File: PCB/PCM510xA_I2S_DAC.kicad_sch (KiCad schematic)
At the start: 30 parts, among them J1 EDGE_PINS, J2 TRS_LINE_OUT, U1 PCM5101A, U2 MIC5225-3.3

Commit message: update to 1.0.0
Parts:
- removed JP1: SCK, Jumper:SolderJumper-3_P1.3mm_Bridged12_RoundedPad1.0x1.5mm, symbol Jumper:SolderJumper_3_Bridged12
- removed TP4: 3.3VA, TestPoint:TestPoint_Pad_2.0x2.0mm, symbol Connector:TestPoint
- removed TP5: LDOO, TestPoint:TestPoint_Pad_2.0x2.0mm, symbol Connector:TestPoint
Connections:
- net SCK is gone; now on net GND: U1.12 (SCK)
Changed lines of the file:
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@@
   (title_block
     (title "PCM510x_I2S_DAC Breakout")
-    (date "2023-10-02")
-    (rev "0.0.2")
+    (date "2023-10-22")
+    (rev "1.0.0")
     (company "Cedar Grove Studios")
   )
@@
   (junction (at 59.69 185.42) (diameter 0) (color 0 0 0 0)
   )
-  (junction (at 148.59 106.68) (diameter 0) (color 0 0 0 0)
-  )
   (junction (at 65.405 167.64) (diameter 0) (color 0 0 0 0)
   )
@@
   )
   (junction (at 194.945 73.66) (diameter 0) (color 0 0 0 0)
+  )
+  (junction (at 111.125 82.55) (diameter 0) (color 0 0 0 0)
   )
   (junction (at 137.16 182.245) (diameter 0) (color 0 0 0 0)
@@
     (stroke (width 0) (type default))
   )
-  (wire (pts (xy 100.965 121.285) (xy 100.965 127.635))
-    (stroke (width 0) (type default))
-  )
   (wire (pts (xy 182.88 89.535) (xy 180.34 89.535))
     (stroke (width 0) (type default))
@@
     (stroke (width 0) (type default))
   )
+  (wire (pts (xy 111.125 82.55) (xy 111.125 77.47))
+    (stroke (width 0) (type default))
+  )
   (wire (pts (xy 148.59 106.68) (xy 157.48 106.68))
     (stroke (width 0) (type default))
@@
     (stroke (width 0) (type default))
   )
+  (wire (pts (xy 111.125 77.47) (xy 124.46 77.47))
+    (stroke (width 0) (type default))
+  )
   (wire (pts (xy 29.845 185.42) (xy 34.29 185.42))
     (stroke (width 0) (type default))
@@
     (stroke (width 0) (type default))
   )
-  (wire (pts (xy 104.775 77.47) (xy 124.46 77.47))
-    (stroke (width 0) (type default))
-  )
   (wire (pts (xy 149.86 72.39) (xy 170.815 72.39))
     (stroke (width 0) (type default))
@@
     (stroke (width 0) (type default))
   )
-  (wire (pts (xy 104.775 77.47) (xy 104.775 116.205))
-    (stroke (width 0) (type default))
-  )
   (wire (pts (xy 170.815 89.535) (xy 175.26 89.535))
     (stroke (width 0) (type default))
@@
   )
   (wire (pts (xy 124.46 87.63) (xy 120.015 87.63))
-    (stroke (width 0) (type default))
-  )
-  (wire (pts (xy 100.965 104.775) (xy 100.965 111.125))
     (stroke (width 0) (type default))
   )
@@
   (label "DIN" (at 93.98 72.39 180) (fields_autoplaced)
     (effects (font (size 1.27 1.27)) (justify right bottom))
-  )
-  (label "SCK" (at 104.775 77.47 0) (fields_autoplaced)
-    (effects (font (size 1.27 1.27)) (justify left bottom))
   )
   (label "Vin" (at 21.59 167.64 0) (fields_autoplaced)
@@
     )
   )
-  (symbol (lib_id "power:GND") (at 100.965 127.635 0) (unit 1)
-    (in_bom yes) (on_board yes) (dnp no)
-    (property "Reference" "#PWR013" (at 100.965 133.985 0)
-      (effects (font (size 1.27 1.27)) hide)
-    )
-    (property "Value" "GND" (at 101.092 132.0292 0)
-      (effects (font (size 1.27 1.27)))
-    )
-    (property "Footprint" "" (at 100.965 127.635 0)
-      (effects (font (size 1.27 1.27)) hide)
-    )
-    (property "Datasheet" "" (at 100.965 127.635 0)
-      (effects (font (size 1.27 1.27)) hide)
-    )
-    (pin "1")
-    (instances
-      (project "PCM510xA_I2S_DAC"
-        (path "/d1262c4d-2245-4c4f-8f35-7bb32cd9e21e"
-          (reference "#PWR013") (unit 1)
-        )
-      )
-    )
-  )
   (symbol (lib_id "power:+3.3VA") (at 113.03 162.56 0) (unit 1)
     (in_bom yes) (on_board yes) (dnp no) (fields_autoplaced)
@@
         (path "/d1262c4d-2245-4c4f-8f35-7bb32cd9e21e"
           (reference "#PWR016") (unit 1)
-        )
-      )
-    )
-  )
-  (symbol (lib_id "Connector:TestPoint") (at 105.41 167.64 0) (unit 1)
-    (in_bom yes) (on_board yes) (dnp no) (fields_autoplaced)
-    (property "Reference" "TP4" (at 106.807 163.1259 0)
-      (effects (font (size 1.27 1.27)) (justify left))
-    )
-    (property "Value" "3.3VA" (at 106.807 165.5501 0)
-      (effects (font (size 1.27 1.27)) (justify left))
-    )
-    (property "Footprint" "TestPoint:TestPoint_Pad_2.0x2.0mm" (at 110.49 167.64 0)
-      (effects (font (size 1.27 1.27)) hide)
-    )
-    (property "Datasheet" "~" (at 110.49 167.64 0)
-      (effects (font (size 1.27 1.27)) hide)
-    )
-    (pin "1")
-    (instances
-      (project "PCM510xA_I2S_DAC"
-        (path "/d1262c4d-2245-4c4f-8f35-7bb32cd9e21e"
-          (reference "TP4") (unit 1)
         )
       )
@@
     )
   )
-  (symbol (lib_id "Connector:TestPoint") (at 148.59 106.68 0) (unit 1)
-    (in_bom yes) (on_board yes) (dnp no) (fields_autoplaced)
-    (property "Reference" "TP5" (at 149.987 102.1659 0)
-      (effects (font (size 1.27 1.27)) (justify left))
-    )
-    (property "Value" "LDOO" (at 149.987 104.5901 0)
-      (effects (font (size 1.27 1.27)) (justify left))
-    )
-    (property "Footprint" "TestPoint:TestPoint_Pad_2.0x2.0mm" (at 153.67 106.68 0)
-      (effects (font (size 1.27 1.27)) hide)
-    )
-    (property "Datasheet" "~" (at 153.67 106.68 0)
-      (effects (font (size 1.27 1.27)) hide)
-    )
-    (pin "1")
-    (instances
-      (project "PCM510xA_I2S_DAC"
-        (path "/d1262c4d-2245-4c4f-8f35-7bb32cd9e21e"
-          (reference "TP5") (unit 1)
-        )
-      )
-    )
-  )
   (symbol (lib_id "power:GND") (at 83.185 190.5 0) (unit 1)
     (in_bom yes) (on_board yes) (dnp no)
@@
     )
   )
-  (symbol (lib_id "Jumper:SolderJumper_3_Bridged12") (at 100.965 116.205 90) (unit 1)
-    (in_bom yes) (on_board yes) (dnp no) (fields_autoplaced)
-    (property "Reference" "JP1" (at 99.3141 114.9929 90)
-      (effects (font (size 1.27 1.27)) (justify left))
-    )
-    (property "Value" "SCK" (at 99.3141 117.4171 90)
-      (effects (font (size 1.27 1.27)) (justify left))
-    )
-    (property "Footprint" "Jumper:SolderJumper-3_P1.3mm_Bridged12_RoundedPad1.0x1.5mm" (at 100.965 116.205 0)
-      (effects (font (size 1.27 1.27)) hide)
-    )
-    (property "Datasheet" "~" (at 100.965 116.205 0)
-      (effects (font (size 1.27 1.27)) hide)
-    )
-    (pin "1")
-    (pin "2")
-    (pin "3")
-    (instances
-      (project "PCM510xA_I2S_DAC"
-        (path "/d1262c4d-2245-4c4f-8f35-7bb32cd9e21e"
-          (reference "JP1") (unit 1)
-        )
-      )
-    )
-  )
   (symbol (lib_id "power:+3.3VA") (at 161.925 40.64 0) (unit 1)
     (in_bom yes) (on_board yes) (dnp no) (fields_autoplaced)
@@
         )
       )
-    )
-  )
-  (symbol (lib_id "power:+3.3V") (at 100.965 104.775 0) (unit 1)
-    (in_bom yes) (on_board yes) (dnp no) (fields_autoplaced)
-    (property "Reference" "#PWR011" (at 100.965 108.585 0)
-      (effects (font (size 1.27 1.27)) hide)
-    )
-    (property "Value" "+3.3V" (at 100.965 100.6419 0)
-      (effects (font (size 1.27 1.27)))
-    )
-    (property "Footprint" "" (at 100.965 104.775 0)
-      (effects (font (size 1.27 1.27)) hide)
-    )
-    (property "Datasheet" "" (at 100.965 104.775 0)
-      (effects (font (size 1.27 1.27)) hide)
-    )
-    (pin "1")
-    (instances
-      (project "PCM510xA_I2S_DAC"
-        (path "/d1262c4d-2245-4c4f-8f35-7bb32cd9e21e"
-          (reference "#PWR011") (unit 1)
-        )
-      )

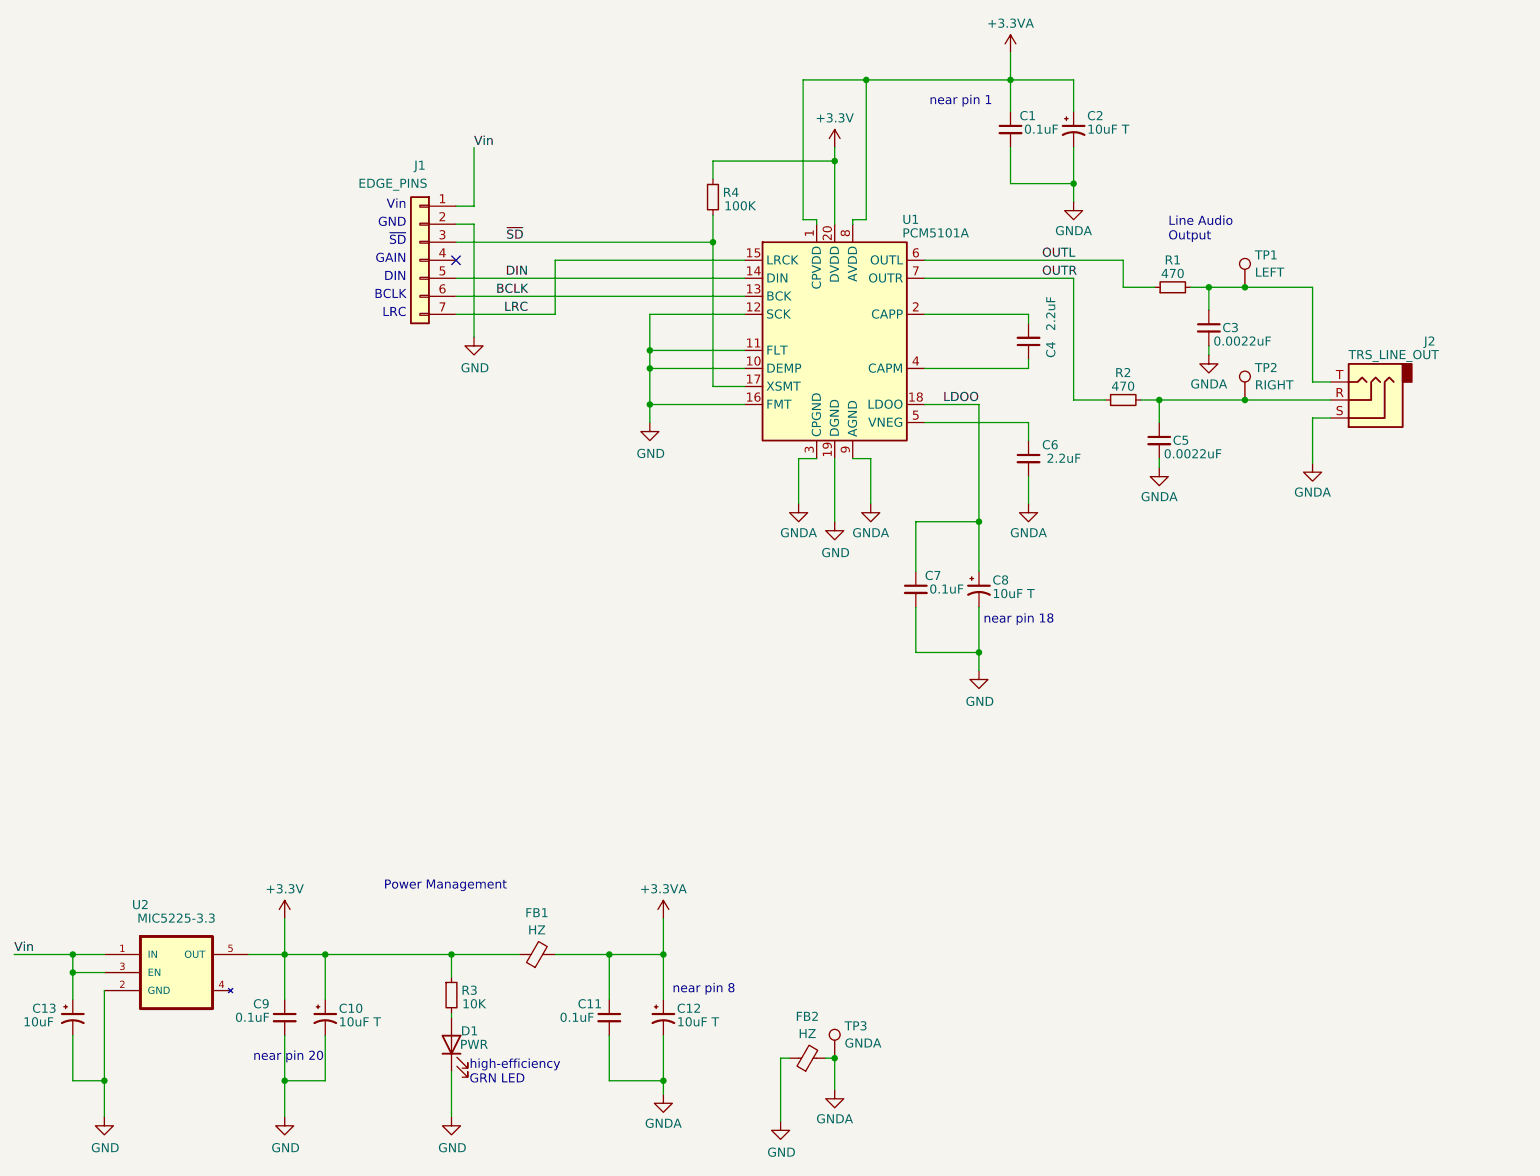
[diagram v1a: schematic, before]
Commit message: update 3.3v regulator
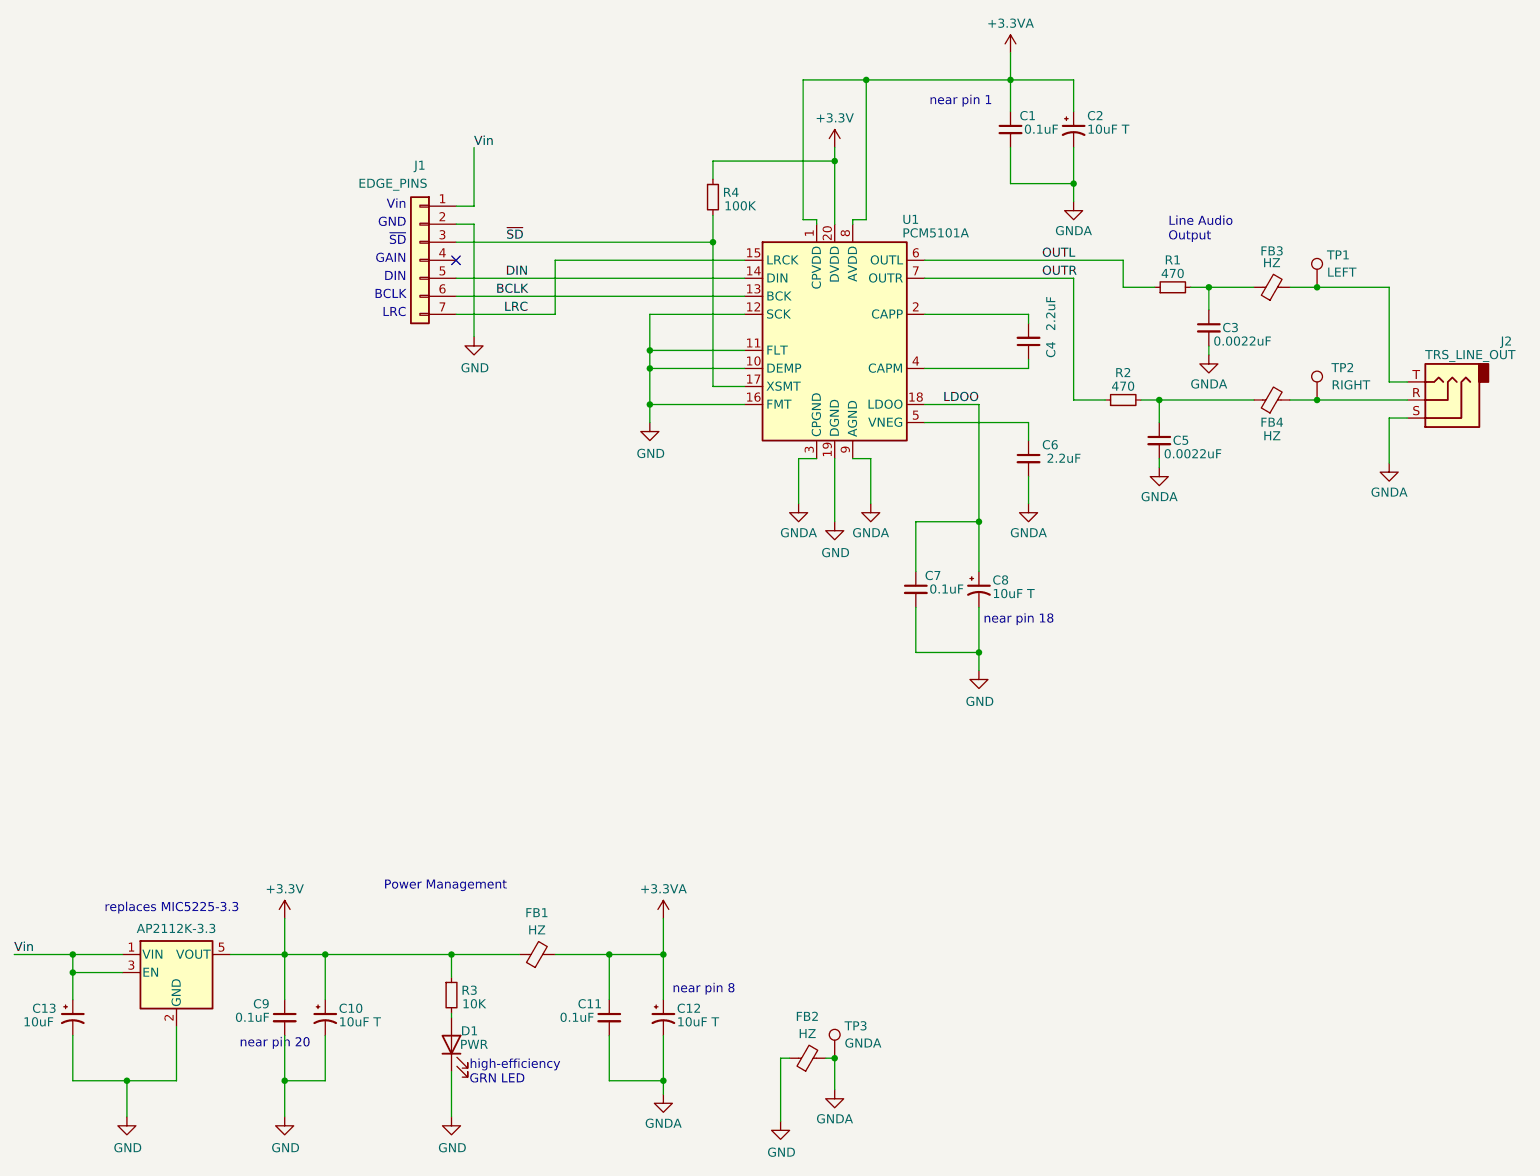
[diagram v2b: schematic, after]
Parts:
- removed U2: MIC5225-3.3, Package_TO_SOT_SMD:SOT-23-5, symbol Regulator_Linear:MIC5225-3.3YM5
- added FB3, FB4: HZ, Resistor_SMD:R_0805_2012Metric, symbol Device:FerriteBead_Small
- added U2: AP2112K-3.3, Package_TO_SOT_SMD:SOT-23-5, symbol Regulator_Linear:AP2112K-3.3
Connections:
- net +3.3V: now also U2.5 (VOUT)
- net GND: now also U2.2 (GND)
- net Vin: now also U2.1 (VIN), U2.3 (EN)
- net at C5.1, R2.2: now also FB4.1; no longer J2.R, TP2.1
- net at C3.1, R1.2: now also FB3.1; no longer J2.T, TP1.1
- new net: FB3.2, J2.T, TP1.1
- new net: FB4.2, J2.R, TP2.1
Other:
- note added: "replaces MIC5225-3.3"
- moved on the sheet: J2, TP1, TP2
